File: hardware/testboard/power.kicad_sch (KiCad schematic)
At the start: 5 parts, among them J12 Reset, P8 Conn_01x06, P9 Conn_01x06

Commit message: work on testboard, move 3d models
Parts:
- removed C57, C58: 220uF, symbol Device:C_Polarized_US
- removed J12: Reset, Connector_PinHeader_2.54mm:PinHeader_1x02_P2.54mm_Vertical, symbol Connector_Generic:Conn_01x02
- removed P8, P9: Conn_01x06, 68040:15-48-0106, symbol Connector_Generic:Conn_01x06
- added C28, C29: 220uF, symbol Device:C_Polarized_US
- added J1: Reset, Connector_PinHeader_2.54mm:PinHeader_1x02_P2.54mm_Vertical, symbol Connector_Generic:Conn_01x02
- added P1, P2: Conn_01x06, 68040:15-48-0106, symbol Connector_Generic:Conn_01x06
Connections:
- net +12V: now also C29.1, P1.3 (Pin_3)
- net +5V: now also C28.1, P1.2 (Pin_2), P2.4 (Pin_4), P2.5 (Pin_5), P2.6 (Pin_6)
- net -12V: now also P1.4 (Pin_4)
- net -5V: now also P2.3 (Pin_3)
- net GND: now also C28.2, C29.2, J1.2 (Pin_2), P1.5 (Pin_5), P1.6 (Pin_6), P2.1 (Pin_1), P2.2 (Pin_2)
- net PWR_GOOD: now also P1.1 (Pin_1)

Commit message: simpleboard nearly complete
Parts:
- removed C29: 220uF, symbol Device:C_Polarized_US
- removed J1: Reset, Connector_PinHeader_2.54mm:PinHeader_1x02_P2.54mm_Vertical, symbol Connector_Generic:Conn_01x02
- removed P1, P2: Conn_01x06, 68040:15-48-0106, symbol Connector_Generic:Conn_01x06
- added C64, C65, C66, C67: 4.7uF, Capacitor_SMD:C_0603_1608Metric, symbol Device:C_Small
- added J1: Barrel_Jack, Connector_BarrelJack:BarrelJack_GCT_DCJ200-10-A_Horizontal, symbol Connector:Barrel_Jack
- added U20: AP2112K-3.3, Package_TO_SOT_SMD:SOT-23-5, symbol Regulator_Linear:AP2112K-3.3
- added U21: AP2112K-1.2, Package_TO_SOT_SMD:SOT-23-5, symbol Regulator_Linear:AP2112K-1.2
- C28: footprint (none) -> Capacitor_THT:CP_Radial_D8.0mm_P2.50mm
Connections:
- net +5V: now also C64.1, C66.1, J1.1, U20.1 (VIN), U20.3 (EN), U21.1 (VIN), U21.3 (EN)
- net GND: now also C64.2, C65.2, C66.2, C67.2, J1.2, U20.2 (GND), U21.2 (GND)
- new net +1V2: C67.1, U21.5 (VOUT)
- new net +3.3V: C65.1, U20.5 (VOUT)
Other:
- moved on the sheet: C28

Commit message: pinouts
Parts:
- renumbered C64 to C701, C66 to C702, C65 to C703, C67 to C704, C28 to C705, J1 to J701, U20 to U701, U21 to U702
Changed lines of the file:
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@@
   (symbol (lib_id "power:GND") (at 63.5 137.16 0) (unit 1)
     (in_bom yes) (on_board yes) (dnp no) (fields_autoplaced)
-    (property "Reference" "#PWR0126" (at 63.5 143.51 0)
+    (property "Reference" "#PWR0703" (at 63.5 143.51 0)
       (effects (font (size 1.27 1.27)) hide)
     )
@@
       (project "testboard"
         (path "/a1ce156a-fb78-423b-b05a-d07384e5c8a7/6a2b0558-9bb2-48d3-955c-fa9d5ac4aef2"
-          (reference "#PWR0126") (unit 1)
+          (reference "#PWR0703") (unit 1)
         )
       )
@@
   (symbol (lib_id "power:+3.3V") (at 78.74 127 0) (unit 1)
     (in_bom yes) (on_board yes) (dnp no) (fields_autoplaced)
-    (property "Reference" "#PWR0122" (at 78.74 130.81 0)
+    (property "Reference" "#PWR0705" (at 78.74 130.81 0)
       (effects (font (size 1.27 1.27)) hide)
     )
@@
       (project "testboard"
         (path "/a1ce156a-fb78-423b-b05a-d07384e5c8a7/6a2b0558-9bb2-48d3-955c-fa9d5ac4aef2"
-          (reference "#PWR0122") (unit 1)
+          (reference "#PWR0705") (unit 1)
         )
       )
@@
   (symbol (lib_id "power:+1V2") (at 78.74 154.94 0) (unit 1)
     (in_bom yes) (on_board yes) (dnp no) (fields_autoplaced)
-    (property "Reference" "#PWR0128" (at 78.74 158.75 0)
+    (property "Reference" "#PWR0706" (at 78.74 158.75 0)
       (effects (font (size 1.27 1.27)) hide)
     )
@@
       (project "testboard"
         (path "/a1ce156a-fb78-423b-b05a-d07384e5c8a7/6a2b0558-9bb2-48d3-955c-fa9d5ac4aef2"
-          (reference "#PWR0128") (unit 1)
+          (reference "#PWR0706") (unit 1)
         )
       )
@@
   (symbol (lib_id "power:+5V") (at 45.72 127 0) (unit 1)
     (in_bom yes) (on_board yes) (dnp no) (fields_autoplaced)
-    (property "Reference" "#PWR09" (at 45.72 130.81 0)
+    (property "Reference" "#PWR0701" (at 45.72 130.81 0)
       (effects (font (size 1.27 1.27)) hide)
     )
@@
       (project "testboard"
         (path "/a1ce156a-fb78-423b-b05a-d07384e5c8a7/6a2b0558-9bb2-48d3-955c-fa9d5ac4aef2"
-          (reference "#PWR09") (unit 1)
+          (reference "#PWR0701") (unit 1)
         )
       )
@@
   (symbol (lib_id "Connector:Barrel_Jack") (at 101.6 83.82 0) (unit 1)
     (in_bom yes) (on_board yes) (dnp no) (fields_autoplaced)
-    (property "Reference" "J1" (at 101.6 74.93 0)
+    (property "Reference" "J701" (at 101.6 74.93 0)
       (effects (font (size 1.27 1.27)))
     )
@@
       (project "testboard"
         (path "/a1ce156a-fb78-423b-b05a-d07384e5c8a7/6a2b0558-9bb2-48d3-955c-fa9d5ac4aef2"
-          (reference "J1") (unit 1)
+          (reference "J701") (unit 1)
         )
       )
@@
   (symbol (lib_id "Regulator_Linear:AP2112K-3.3") (at 63.5 129.54 0) (unit 1)
     (in_bom yes) (on_board yes) (dnp no) (fields_autoplaced)
-    (property "Reference" "U20" (at 63.5 120.65 0)
+    (property "Reference" "U701" (at 63.5 120.65 0)
       (effects (font (size 1.27 1.27)))
     )
@@
       (project "testboard"
         (path "/a1ce156a-fb78-423b-b05a-d07384e5c8a7/6a2b0558-9bb2-48d3-955c-fa9d5ac4aef2"
-          (reference "U20") (unit 1)
+          (reference "U701") (unit 1)
         )
       )
@@
   (symbol (lib_id "Regulator_Linear:AP2112K-1.2") (at 63.5 157.48 0) (unit 1)
     (in_bom yes) (on_board yes) (dnp no) (fields_autoplaced)
-    (property "Reference" "U21" (at 63.5 148.59 0)
+    (property "Reference" "U702" (at 63.5 148.59 0)
       (effects (font (size 1.27 1.27)))
     )
@@
       (project "testboard"
         (path "/a1ce156a-fb78-423b-b05a-d07384e5c8a7/6a2b0558-9bb2-48d3-955c-fa9d5ac4aef2"
-          (reference "U21") (unit 1)
+          (reference "U702") (unit 1)
         )
       )
@@
   (symbol (lib_id "power:GND") (at 132.08 88.9 0) (unit 1)
     (in_bom yes) (on_board yes) (dnp no) (fields_autoplaced)
-    (property "Reference" "#PWR053" (at 132.08 95.25 0)
+    (property "Reference" "#PWR0708" (at 132.08 95.25 0)
       (effects (font (size 1.27 1.27)) hide)
     )
@@
       (project "testboard"
         (path "/a1ce156a-fb78-423b-b05a-d07384e5c8a7/6a2b0558-9bb2-48d3-955c-fa9d5ac4aef2"
-          (reference "#PWR053") (unit 1)
+          (reference "#PWR0708") (unit 1)
         )
       )
@@
   (symbol (lib_id "power:GND") (at 63.5 165.1 0) (unit 1)
     (in_bom yes) (on_board yes) (dnp no) (fields_autoplaced)
-    (property "Reference" "#PWR0133" (at 63.5 171.45 0)
+    (property "Reference" "#PWR0704" (at 63.5 171.45 0)
       (effects (font (size 1.27 1.27)) hide)
     )
@@
       (project "testboard"
         (path "/a1ce156a-fb78-423b-b05a-d07384e5c8a7/6a2b0558-9bb2-48d3-955c-fa9d5ac4aef2"
-          (reference "#PWR0133") (unit 1)
+          (reference "#PWR0704") (unit 1)
         )
       )
@@
   (symbol (lib_id "Device:C_Small") (at 73.66 160.02 0) (unit 1)
     (in_bom yes) (on_board yes) (dnp no) (fields_autoplaced)
-    (property "Reference" "C67" (at 76.2 158.7563 0)
+    (property "Reference" "C704" (at 76.2 158.7563 0)
       (effects (font (size 1.27 1.27)) (justify left))
     )
@@
       (project "testboard"
         (path "/a1ce156a-fb78-423b-b05a-d07384e5c8a7/6a2b0558-9bb2-48d3-955c-fa9d5ac4aef2"
-          (reference "C67") (unit 1)
+          (reference "C704") (unit 1)
         )
       )
@@
   (symbol (lib_id "Device:C_Small") (at 48.26 160.02 0) (unit 1)
     (in_bom yes) (on_board yes) (dnp no) (fields_autoplaced)
-    (property "Reference" "C66" (at 50.8 158.7563 0)
+    (property "Reference" "C702" (at 50.8 158.7563 0)
       (effects (font (size 1.27 1.27)) (justify left))
     )
@@
       (project "testboard"
         (path "/a1ce156a-fb78-423b-b05a-d07384e5c8a7/6a2b0558-9bb2-48d3-955c-fa9d5ac4aef2"
-          (reference "C66") (unit 1)
+          (reference "C702") (unit 1)
         )
       )
@@
   (symbol (lib_id "power:PWR_FLAG") (at 119.38 81.28 0) (unit 1)
     (in_bom yes) (on_board yes) (dnp no) (fields_autoplaced)
-    (property "Reference" "#FLG01" (at 119.38 79.375 0)
+    (property "Reference" "#FLG0701" (at 119.38 79.375 0)
       (effects (font (size 1.27 1.27)) hide)
     )
@@
       (project "testboard"
         (path "/a1ce156a-fb78-423b-b05a-d07384e5c8a7/6a2b0558-9bb2-48d3-955c-fa9d5ac4aef2"
-          (reference "#FLG01") (unit 1)
+          (reference "#FLG0701") (unit 1)
         )
       )
@@
   (symbol (lib_id "power:+5V") (at 132.08 81.28 0) (unit 1)
     (in_bom yes) (on_board yes) (dnp no) (fields_autoplaced)
-    (property "Reference" "#PWR051" (at 132.08 85.09 0)
+    (property "Reference" "#PWR0707" (at 132.08 85.09 0)
       (effects (font (size 1.27 1.27)) hide)
     )
@@
       (project "testboard"
         (path "/a1ce156a-fb78-423b-b05a-d07384e5c8a7/6a2b0558-9bb2-48d3-955c-fa9d5ac4aef2"
-          (reference "#PWR051") (unit 1)
+          (reference "#PWR0707") (unit 1)
         )
       )
@@
   (symbol (lib_id "power:+5V") (at 45.72 154.94 0) (unit 1)
     (in_bom yes) (on_board yes) (dnp no) (fields_autoplaced)
-    (property "Reference" "#PWR0127" (at 45.72 158.75 0)
+    (property "Reference" "#PWR0702" (at 45.72 158.75 0)
       (effects (font (size 1.27 1.27)) hide)
     )
@@
       (project "testboard"
         (path "/a1ce156a-fb78-423b-b05a-d07384e5c8a7/6a2b0558-9bb2-48d3-955c-fa9d5ac4aef2"
-          (reference "#PWR0127") (unit 1)
+          (reference "#PWR0702") (unit 1)
         )
       )
@@
   (symbol (lib_id "Device:C_Polarized_US") (at 132.08 85.09 0) (unit 1)
     (in_bom yes) (on_board yes) (dnp no) (fields_autoplaced)
-    (property "Reference" "C28" (at 135.89 83.185 0)
+    (property "Reference" "C705" (at 135.89 83.185 0)
       (effects (font (size 1.27 1.27)) (justify left))
     )
@@
       (project "testboard"
         (path "/a1ce156a-fb78-423b-b05a-d07384e5c8a7/6a2b0558-9bb2-48d3-955c-fa9d5ac4aef2"
-          (reference "C28") (unit 1)
+          (reference "C705") (unit 1)
         )
       )
@@
   (symbol (lib_id "Device:C_Small") (at 73.66 132.08 0) (unit 1)
     (in_bom yes) (on_board yes) (dnp no) (fields_autoplaced)
-    (property "Reference" "C65" (at 76.2 130.8163 0)
+    (property "Reference" "C703" (at 76.2 130.8163 0)
       (effects (font (size 1.27 1.27)) (justify left))
     )
@@
       (project "testboard"
         (path "/a1ce156a-fb78-423b-b05a-d07384e5c8a7/6a2b0558-9bb2-48d3-955c-fa9d5ac4aef2"
-          (reference "C65") (unit 1)
+          (reference "C703") (unit 1)
         )
       )
@@
   (symbol (lib_id "Device:C_Small") (at 48.26 132.08 0) (unit 1)
     (in_bom yes) (on_board yes) (dnp no) (fields_autoplaced)
-    (property "Reference" "C64" (at 50.8 130.8163 0)
+    (property "Reference" "C701" (at 50.8 130.8163 0)
       (effects (font (size 1.27 1.27)) (justify left))
     )
@@
       (project "testboard"
         (path "/a1ce156a-fb78-423b-b05a-d07384e5c8a7/6a2b0558-9bb2-48d3-955c-fa9d5ac4aef2"
-          (reference "C64") (unit 1)
-        )
-      )
+          (reference "C701") (unit 1)
+        )
+      )

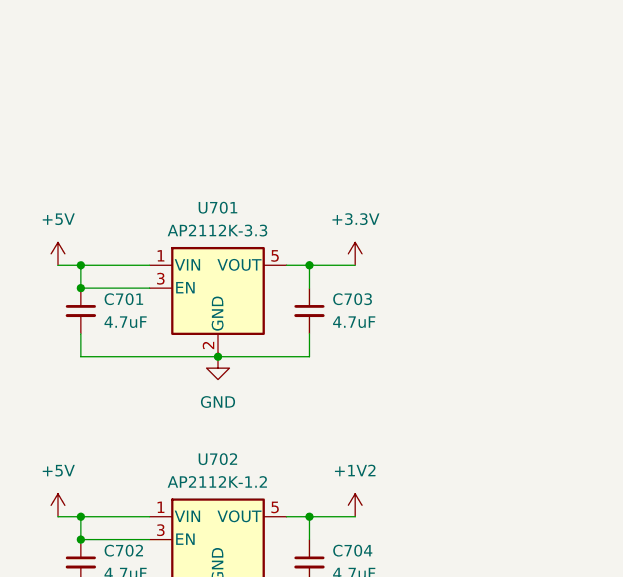
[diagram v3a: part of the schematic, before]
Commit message: make 3.3v reg bigger
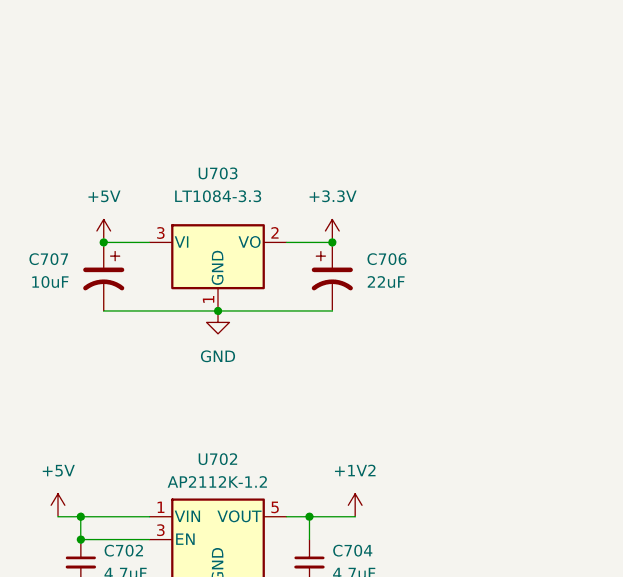
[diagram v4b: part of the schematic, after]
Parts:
- removed C701, C703: 4.7uF, Capacitor_SMD:C_0603_1608Metric, symbol Device:C_Small
- removed U701: AP2112K-3.3, Package_TO_SOT_SMD:SOT-23-5, symbol Regulator_Linear:AP2112K-3.3
- added C706: 22uF, Capacitor_Tantalum_SMD:CP_EIA-2012-12_Kemet-R, symbol Device:C_Polarized_US
- added C707: 10uF, Capacitor_Tantalum_SMD:CP_EIA-2012-12_Kemet-R, symbol Device:C_Polarized_US
- added U703: LT1084-3.3, Package_TO_SOT_SMD:TO-263-3_TabPin2, symbol Regulator_Linear:LT1084-3.3
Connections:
- net +3.3V: now also C706.1, U703.2 (VO)
- net +5V: now also C707.1, U703.3 (VI)
- net GND: now also C706.2, C707.2, U703.1 (GND)
